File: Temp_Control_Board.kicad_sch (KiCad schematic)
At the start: 36 parts, among them J1 OVEN_INTERFACE, J2 OLED, J3 USB_B_Micro, J4 MICROSD, SW1 BOOT, SW2 EN, U1 ESP-WROOM-32, U2 AZ1117EH-3.3TRG1, U3 ROTARY_ENC_PEC12R, U4 FT232RLREEL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

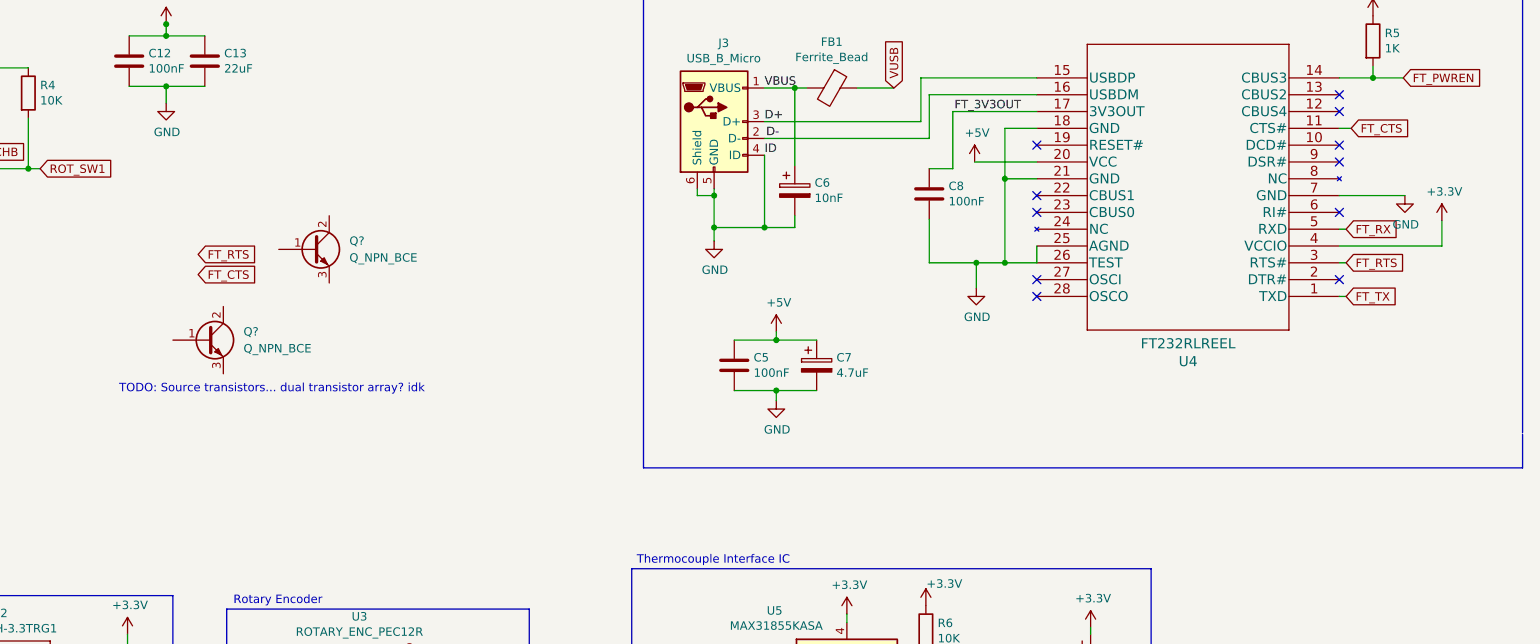
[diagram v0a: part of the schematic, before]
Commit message: sch: Added reset via UART circuit
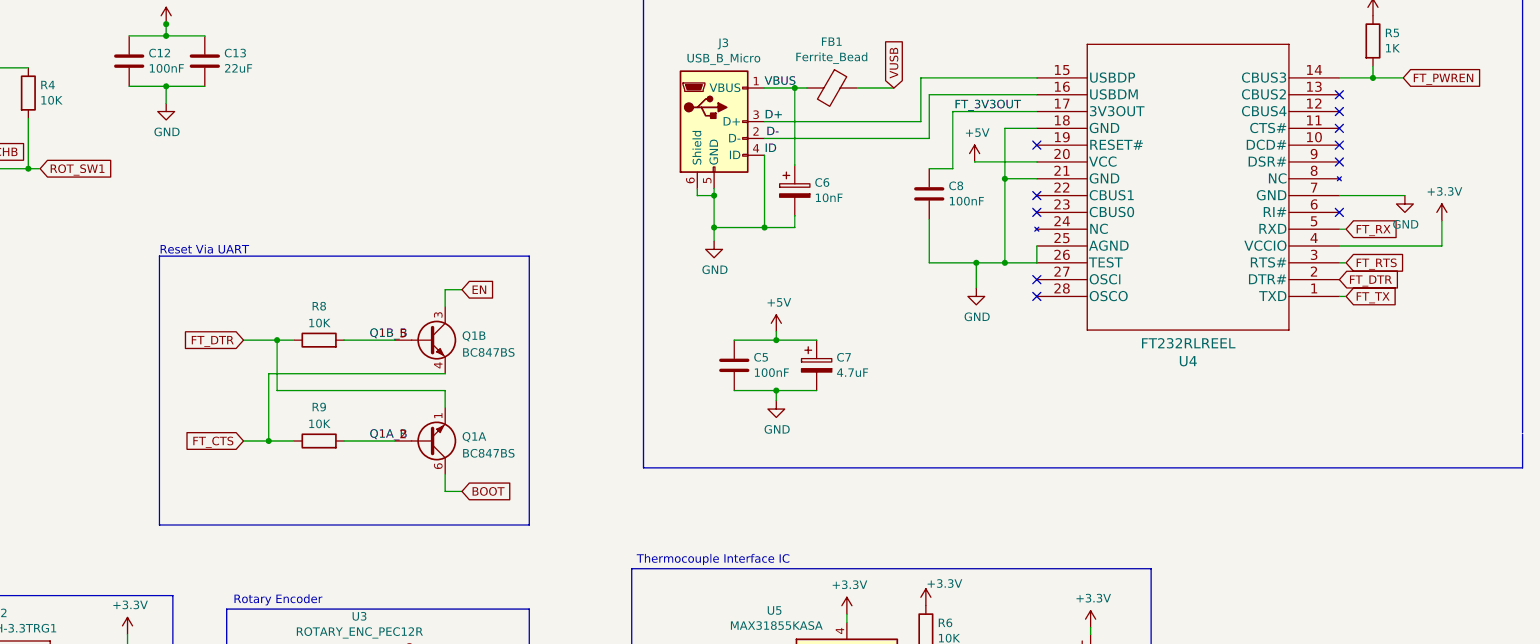
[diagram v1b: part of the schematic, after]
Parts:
- removed Q? (x2): Q_NPN_BCE, symbol Device:Q_NPN_BCE
- added Q1: BC847BS, Package_TO_SOT_SMD:SOT-363_SC-70-6, symbol Transistor_BJT:BC847BS
- added R8, R9: 10K, Resistor_SMD:R_0805_2012Metric_Pad1.20x1.40mm_HandSolder, symbol Device:R
- C1, C10, C12, C13, C2, C3, C4, C5, C6, C7, C8, C9: footprint Capacitor_SMD:C_0805_2012Metric_Pad1.15x1.40mm_HandSolder -> Capacitor_SMD:C_0805_2012Metric_Pad1.18x1.45mm_HandSolder
- FB1, FB2, FB3, R1, R2, R3, R4, R5, R6, R7: footprint Resistor_SMD:R_0805_2012Metric_Pad1.15x1.40mm_HandSolder -> Resistor_SMD:R_0805_2012Metric_Pad1.20x1.40mm_HandSolder
- J2: footprint Display:OLED_1MIL_HEADER_WHOLES -> Connector_PinHeader_2.54mm:PinHeader_1x04_P2.54mm_Vertical
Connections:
- net BOOT: now also Q1.6 (C1)
- net EN: now also Q1.3 (C2)
- net FT_CTS: now also Q1.4 (E2), R9.1; no longer U4.11 (CTS#)
- net FT_DTR: now reaches U4.2 (DTR#)
- net FT_DTR: now also Q1.1 (E1), R8.1
- new net Q1A_B: Q1.2 (B1), R9.2
- new net Q1B_B: Q1.5 (B2), R8.2
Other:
- note added: "Reset Via UART"
- note removed: "TODO: Source transistors... dual transistor array? idk"

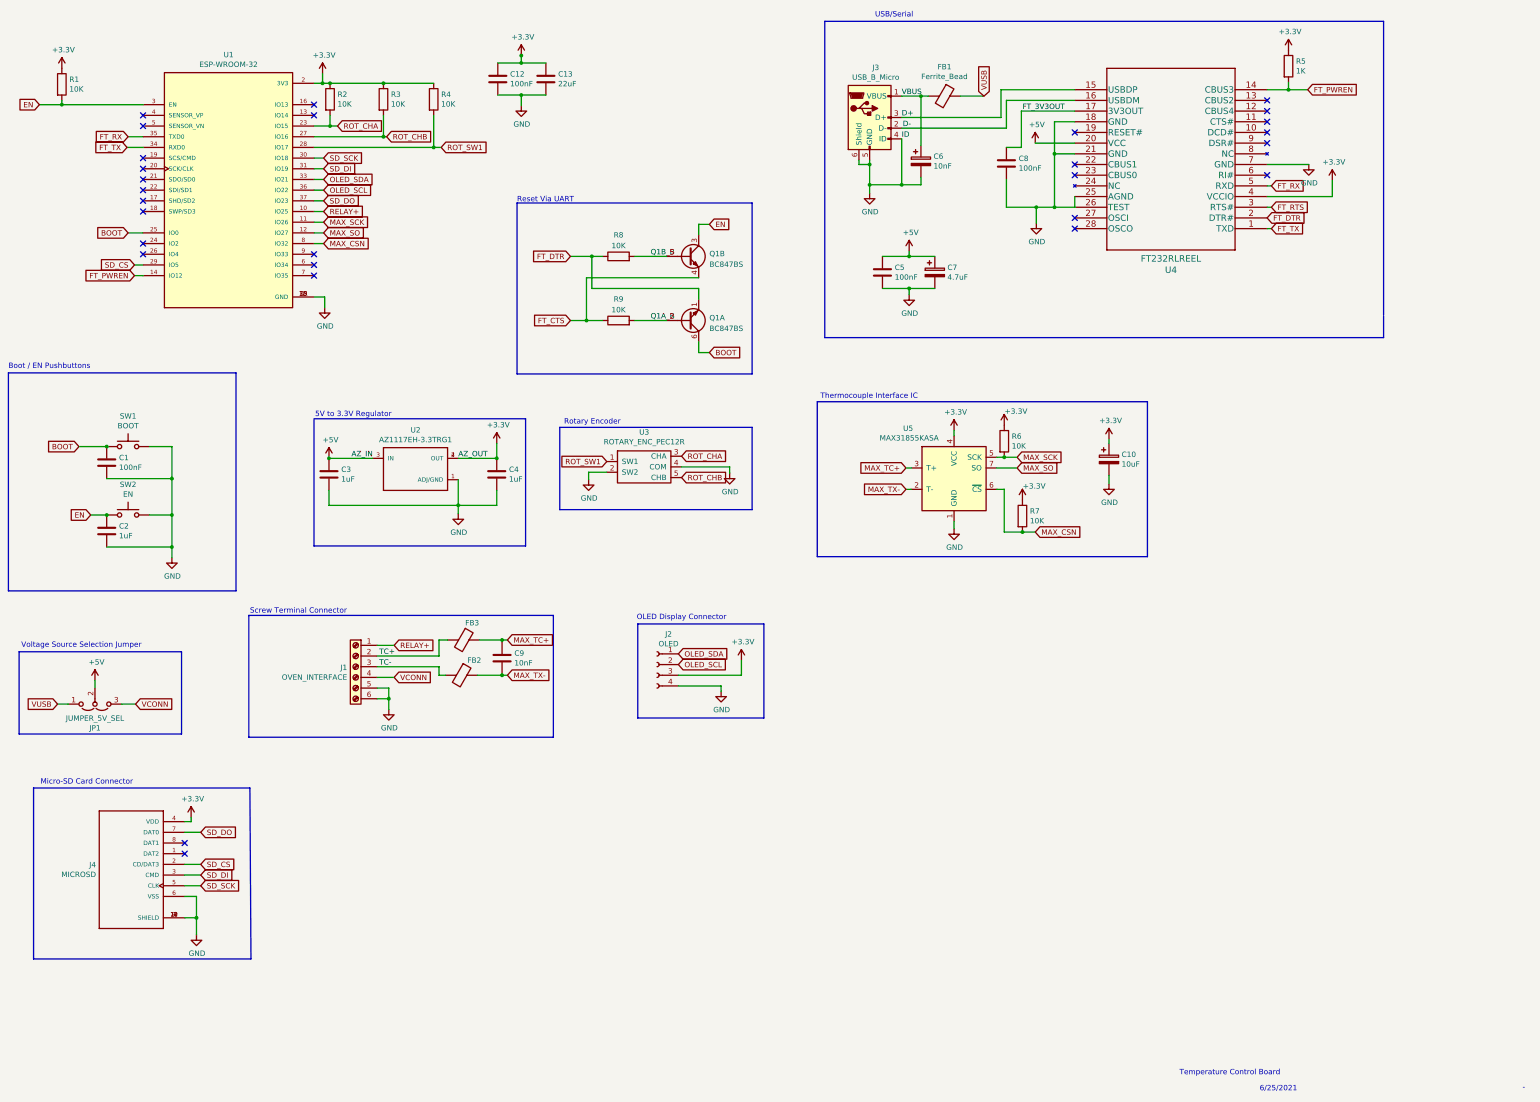
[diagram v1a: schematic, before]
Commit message: sch: Added LEDs
    - Added LEDs for 3.3V, Oven relay enabled, and two
      general purpose LEDs connected to ESP32
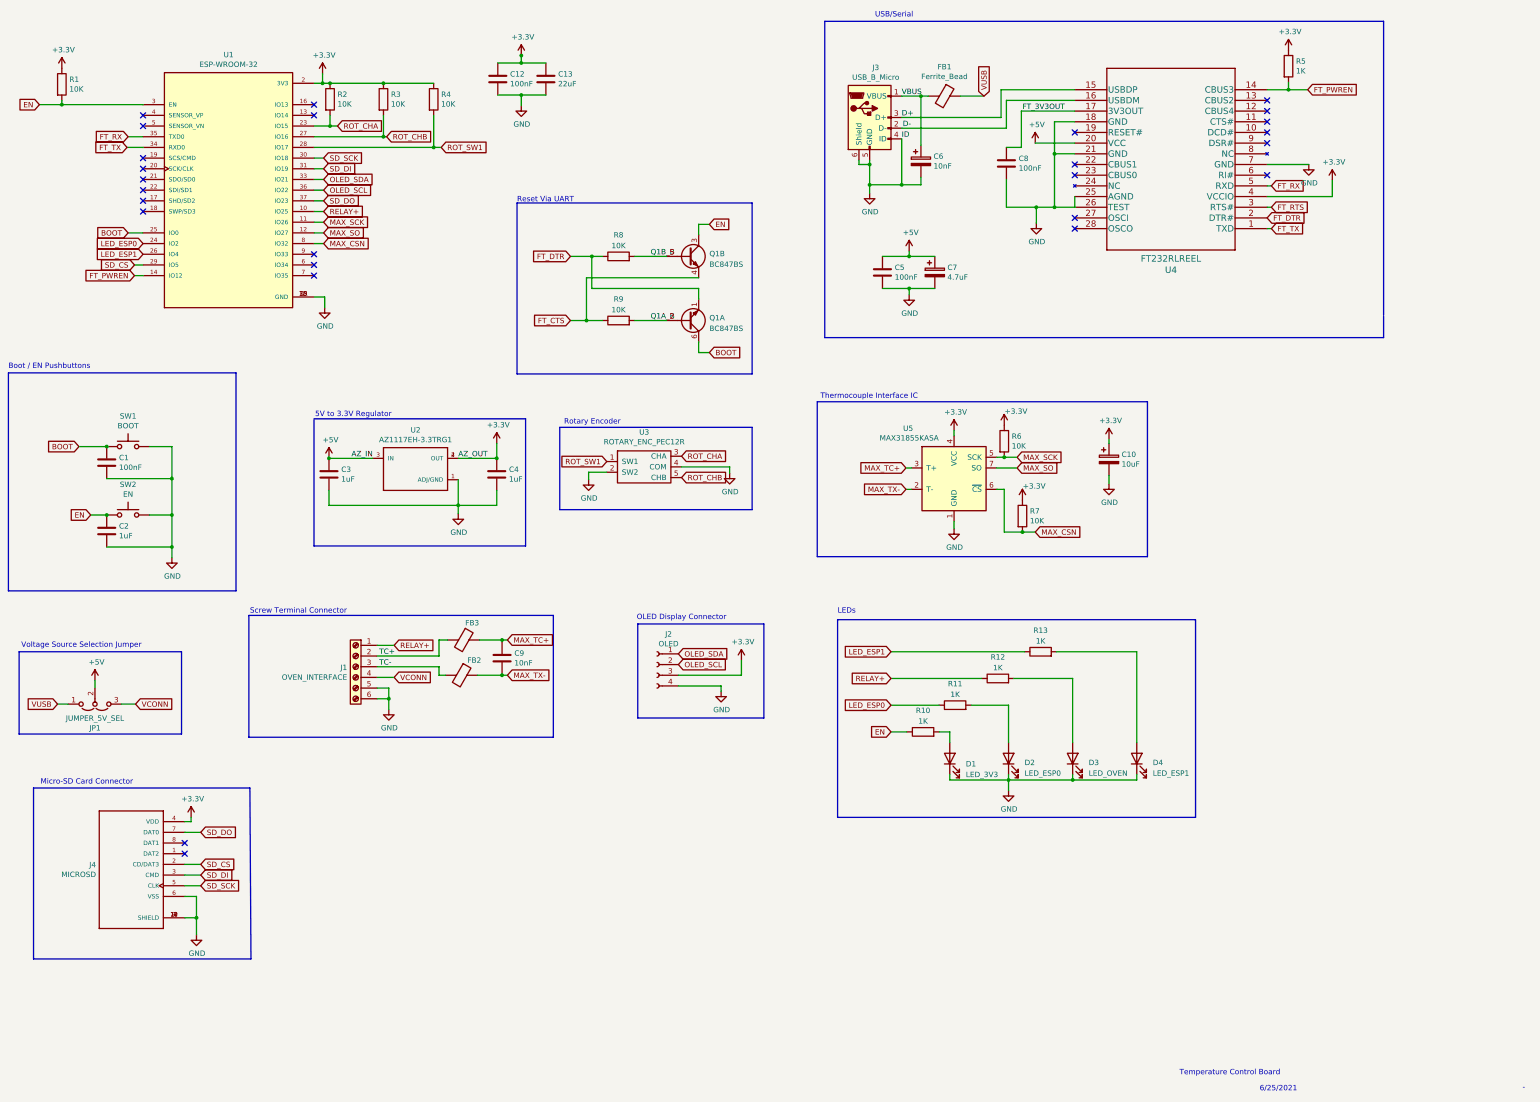
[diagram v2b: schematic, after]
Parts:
- added D1: LED_3V3, LED_SMD:LED_0805_2012Metric_Pad1.15x1.40mm_HandSolder, symbol Device:LED
- added D2: LED_ESP0, LED_SMD:LED_0805_2012Metric_Pad1.15x1.40mm_HandSolder, symbol Device:LED
- added D3: LED_OVEN, LED_SMD:LED_0805_2012Metric_Pad1.15x1.40mm_HandSolder, symbol Device:LED
- added D4: LED_ESP1, LED_SMD:LED_0805_2012Metric_Pad1.15x1.40mm_HandSolder, symbol Device:LED
- added R10, R11, R12, R13: 1K, Resistor_SMD:R_0805_2012Metric_Pad1.20x1.40mm_HandSolder, symbol Device:R
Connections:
- net EN: now also R10.1
- net GND: now also D1.1 (K), D2.1 (K), D3.1 (K), D4.1 (K)
- net RELAY+: now also R12.1
- net LED_ESP0: now reaches U1.24 (IO2)
- net LED_ESP0: now also R11.1
- net LED_ESP1: now reaches U1.26 (IO4)
- net LED_ESP1: now also R13.1
- new net: D3.2 (A), R12.2
- new net: D2.2 (A), R11.2
- new net: D1.2 (A), R10.2
- new net: D4.2 (A), R13.2
- no-connect marks 28 -> 26
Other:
- note added: "LEDs"

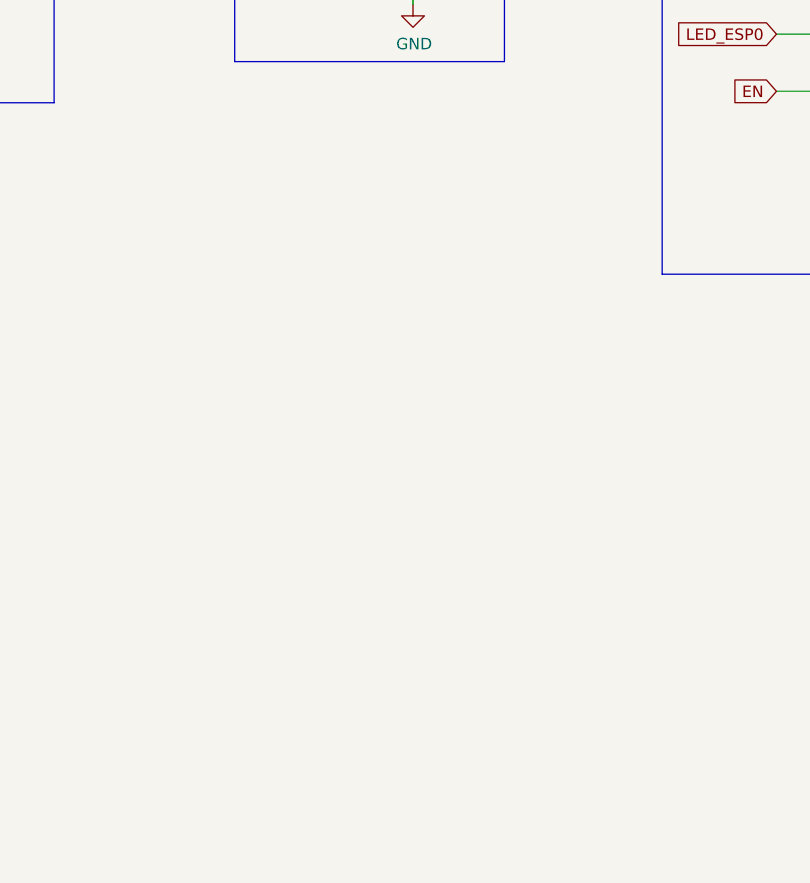
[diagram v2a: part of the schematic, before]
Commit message: sch: added 2.54mm pitch breakout connector
    - Breaks out many signals connected to ESP32
      as well as 3.3V, 5V, and GND
    - Intended for testing or for alternate uses
      of this board
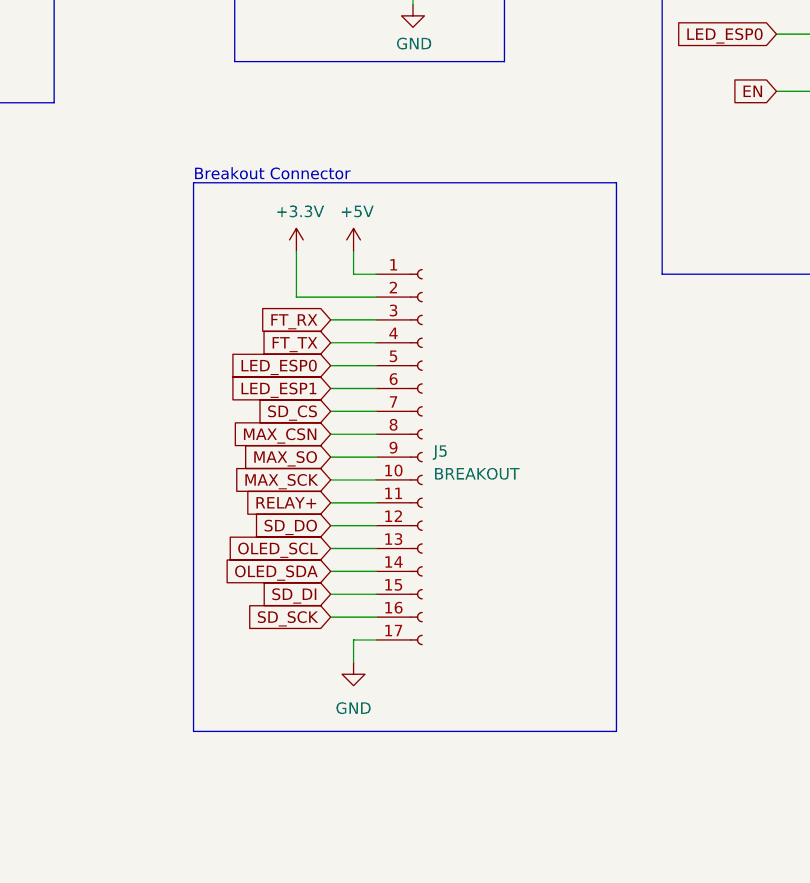
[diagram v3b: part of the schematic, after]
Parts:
- added J5: BREAKOUT, Connector_PinHeader_2.54mm:PinHeader_1x17_P2.54mm_Vertical, symbol Connector:Conn_01x17_Socket
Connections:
- net +3V3: now also J5.2 (Pin_2)
- net +5V: now also J5.1 (Pin_1)
- net FT_RX: now also J5.3 (Pin_3)
- net FT_TX: now also J5.4 (Pin_4)
- net GND: now also J5.17 (Pin_17)
- net LED_ESP0: now also J5.5 (Pin_5)
- net LED_ESP1: now also J5.6 (Pin_6)
- net MAX_CSN: now also J5.8 (Pin_8)
- net MAX_SCK: now also J5.10 (Pin_10)
- net MAX_SO: now also J5.9 (Pin_9)
- net OLED_SCL: now also J5.13 (Pin_13)
- net OLED_SDA: now also J5.14 (Pin_14)
- net RELAY+: now also J5.11 (Pin_11)
- net SD_CS: now also J5.7 (Pin_7)
- net SD_DI: now also J5.15 (Pin_15)
- net SD_DO: now also J5.12 (Pin_12)
- net SD_SCK: now also J5.16 (Pin_16)
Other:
- note added: "Breakout Connector"

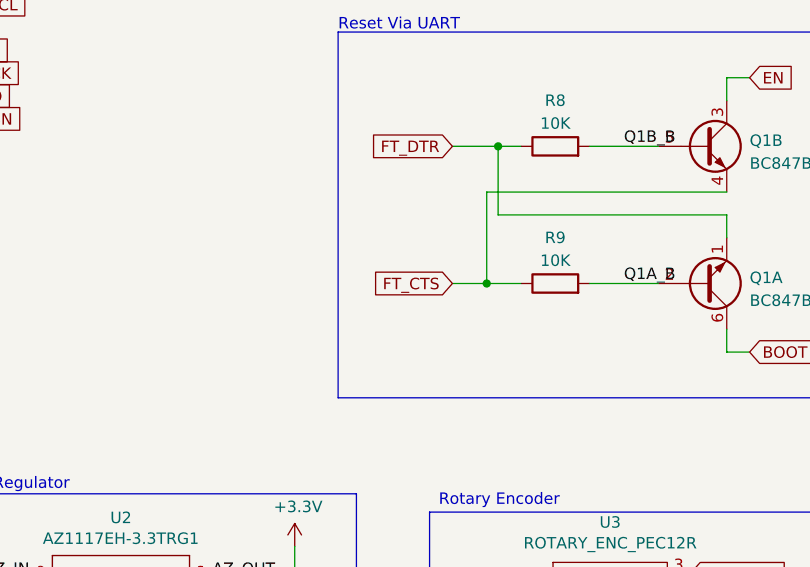
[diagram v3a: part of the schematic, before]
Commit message: pcb: components placed
    - sch: fixed FT_CTS -> FT_RTS on reset circuit
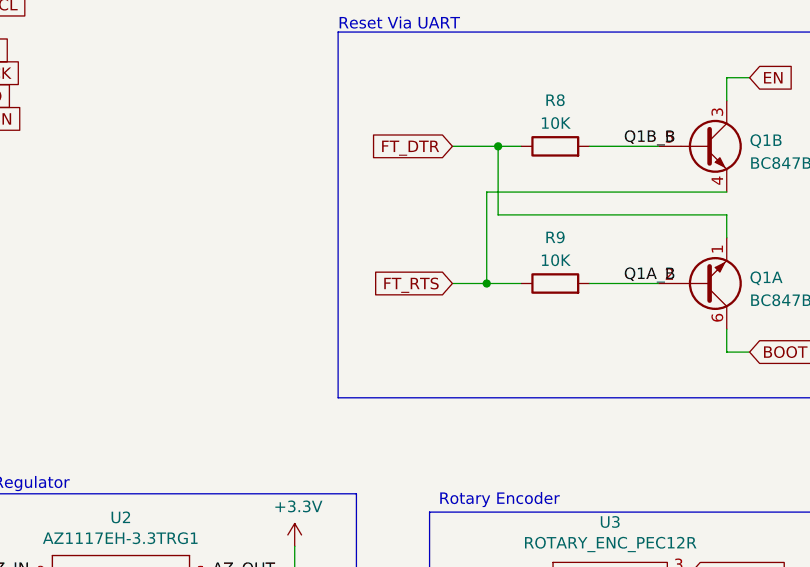
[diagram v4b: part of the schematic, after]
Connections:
- net FT_CTS is gone; now on net FT_RTS: Q1.4 (E2), R9.1
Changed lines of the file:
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@@
-    )
-  )
-  (global_label "FT_CTS" (shape input) (at 165.1 97.79 180) (fields_autoplaced)
-    (effects (font (size 1.27 1.27)) (justify right))
-    (property "Intersheetrefs" "${INTERSHEET_REFS}" (at 156.3775 97.79 0)
-      (effects (font (size 1.27 1.27)) (justify right) hide)
     )
   )
@@
     )
   )
+  (global_label "FT_RTS" (shape input) (at 165.1 97.79 180) (fields_autoplaced)
+    (effects (font (size 1.27 1.27)) (justify right))
+    (property "Intersheetrefs" "${INTERSHEET_REFS}" (at 156.3775 97.79 0)
+      (effects (font (size 1.27 1.27)) (justify right) hide)
+    )
+  )
